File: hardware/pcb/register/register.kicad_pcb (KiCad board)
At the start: 2 copper layers, 62.2 x 21.6 mm, 50 parts, among them J1 Conn_01x08_Male, J2 Conn_01x04_Male, J3 Conn_01x04_Male, J4 Conn_01x04_Male, J5 Conn_01x08_Male, J6 Conn_01x08_Male, U1 74HC245, U2 74HC173, U3 74HC173, U4 74HC173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

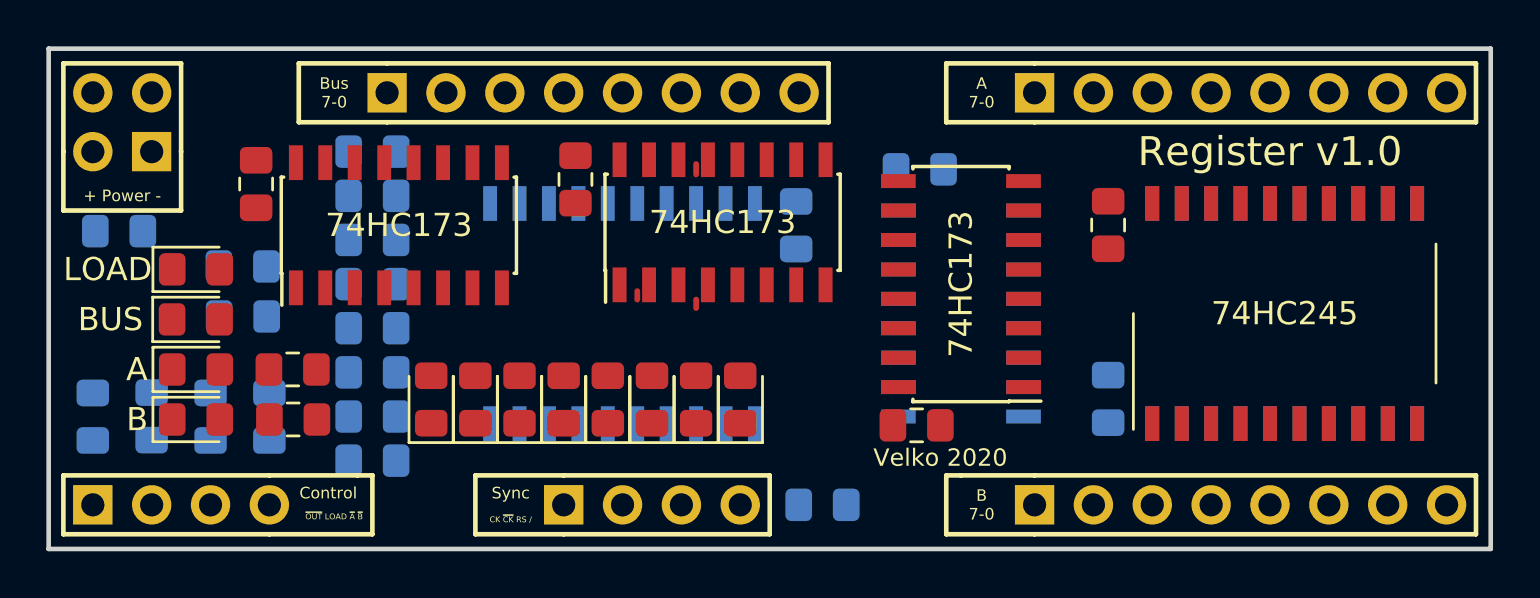
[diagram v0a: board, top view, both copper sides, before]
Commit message: Clean up remaining tracks
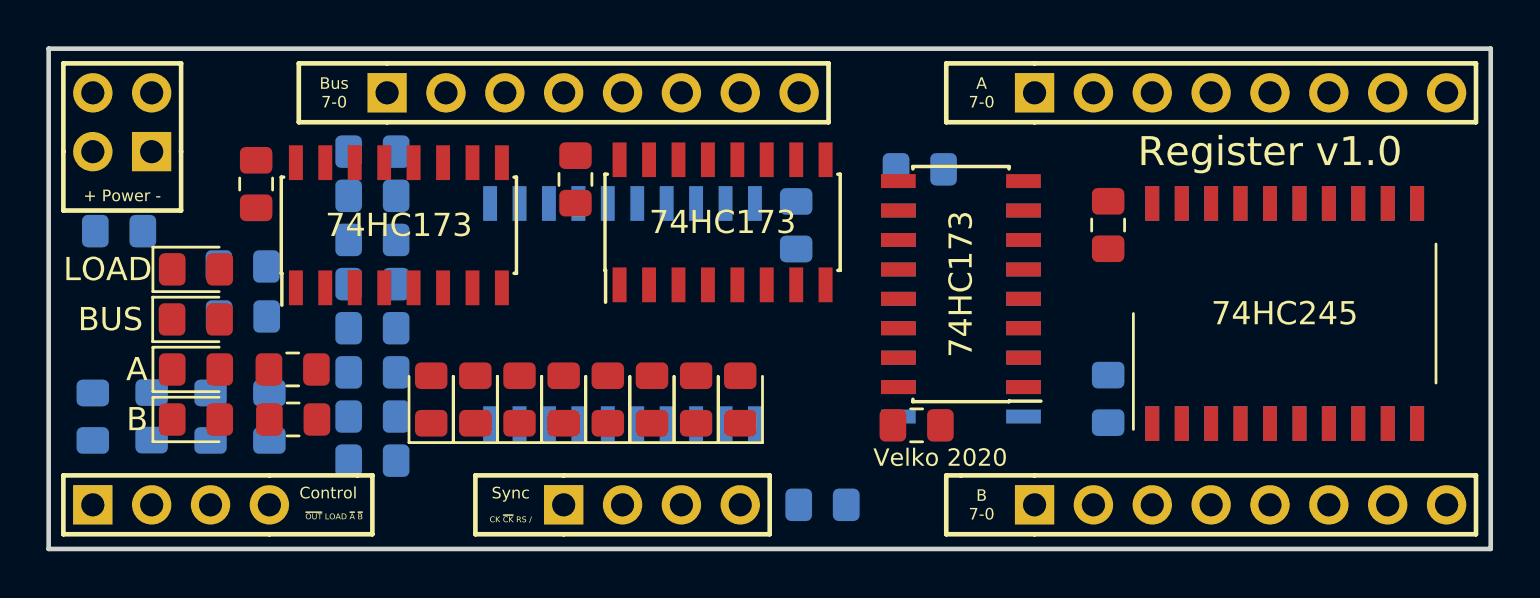
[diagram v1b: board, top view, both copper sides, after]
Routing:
- net A5: track 1.33 -> 0.00 mm
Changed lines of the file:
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@@
     (thickness 1.6)
     (drawings 52)
-    (tracks 11)
+    (tracks 0)
     (zones 0)
     (modules 50)
@@
   (gr_line (start 97.155 36.195) (end 97.155 57.785) (layer Edge.Cuts) (width 0.2))
   (gr_line (start 34.925 36.195) (end 97.155 36.195) (layer Edge.Cuts) (width 0.2))
-  (segment (start 60.325 46.657998) (end 60.325 47.023) (width 0.25) (layer F.Cu) (net 2))
-  (segment (start 53.975 42.875) (end 53.975 42.545) (width 0.25) (layer B.Cu) (net 10))
-  (segment (start 62.865 41.173) (end 62.865 41.623) (width 0.25) (layer F.Cu) (net 15))
-  (segment (start 64.77 38.1) (end 64.75159 38.1) (width 0.25) (layer F.Cu) (net 16))
-  (segment (start 62.865 42.875) (end 62.865 42.545) (width 0.25) (layer B.Cu) (net 17))
-  (segment (start 82.55 38.1) (end 82.55 38.227) (width 0.25) (layer B.Cu) (net 23))
-  (segment (start 83.305 38.1) (end 82.55 38.1) (width 0.25) (layer F.Cu) (net 23))
-  (segment (start 87.63 42.875) (end 87.63 42.425) (width 0.25) (layer F.Cu) (net 23))
-  (segment (start 88.9 52.375) (end 88.9 52.870998) (width 0.25) (layer B.Cu) (net 29))
-  (segment (start 87.665 55.88) (end 87.63 55.88) (width 0.25) (layer B.Cu) (net 30))
-  (segment (start 62.865 47.388002) (end 62.865 47.023) (width 0.25) (layer F.Cu) (net 36))
 )

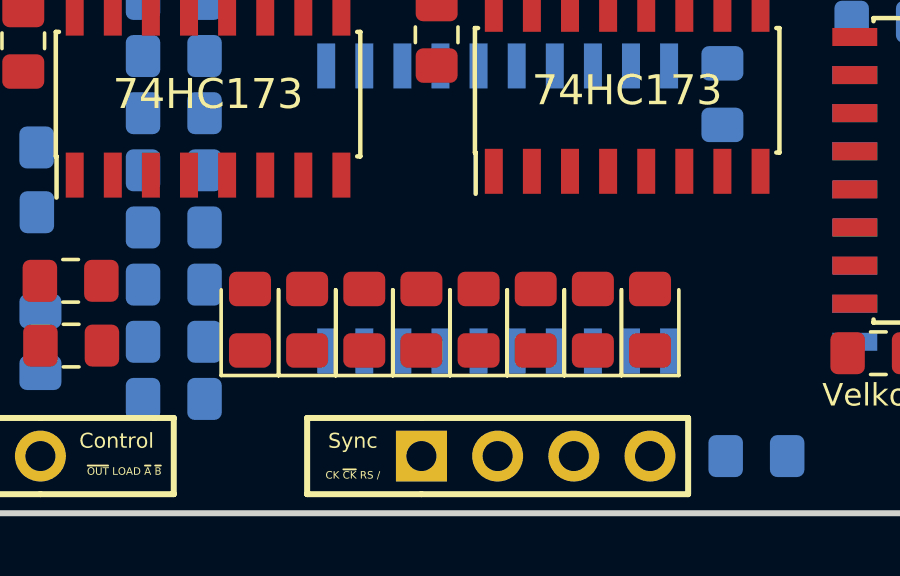
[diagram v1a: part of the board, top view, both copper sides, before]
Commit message: Move LEDs up
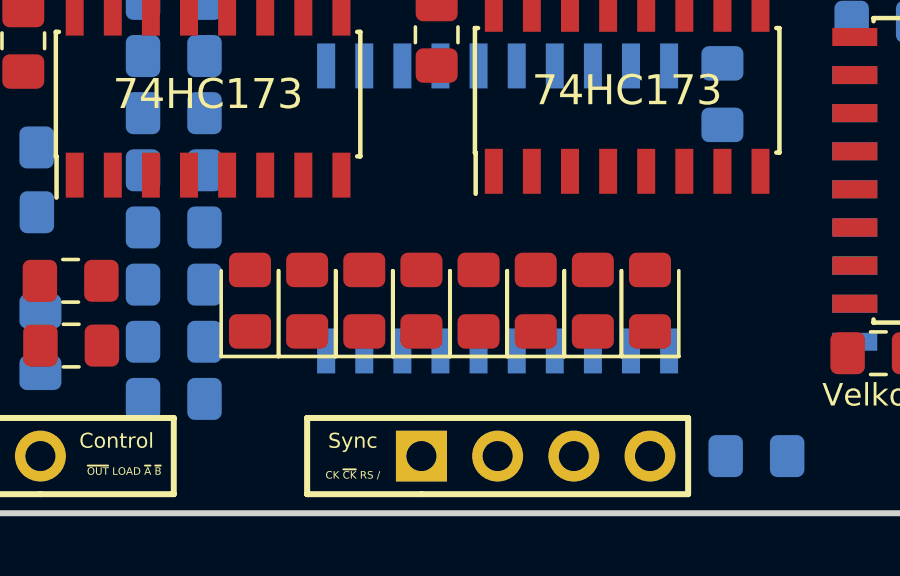
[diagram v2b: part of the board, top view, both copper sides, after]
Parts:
- moved D1 0.63 mm to (64.8, 50.7)
- moved D2 0.63 mm to (62.9, 50.7)
- moved D3 0.63 mm to (61.0, 50.7)
- moved D4 0.63 mm to (59.1, 50.7)
- moved D5 0.63 mm to (57.1, 50.7)
- moved D6 0.63 mm to (55.2, 50.7)
- moved D7 0.63 mm to (53.3, 50.7)
- moved D8 0.63 mm to (51.4, 50.7)
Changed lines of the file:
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@@
   )
   (module LED_SMD:LED_0805_2012Metric_Pad1.15x1.40mm_HandSolder (layer F.Cu)
-    (at 64.77 51.335 90)
+    (at 64.77 50.7 90)
     (descr "LED SMD 0805 (2012 Metric), square (rectangular) end terminal, IPC_7351 nominal, (Body size source: https://docs.google.com/spreadsheets/d/1BsfQQcO9C6DZCsRaXUlFlo91Tg2WpOkGARC1WS5S8t0/edit?usp=sharing), generated with kicad-footprint-generator")
     (tags "LED handsolder")
@@
   )
   (module LED_SMD:LED_0805_2012Metric_Pad1.15x1.40mm_HandSolder (layer F.Cu)
-    (at 62.865 51.335 90)
+    (at 62.865 50.7 90)
     (descr "LED SMD 0805 (2012 Metric), square (rectangular) end terminal, IPC_7351 nominal, (Body size source: https://docs.google.com/spreadsheets/d/1BsfQQcO9C6DZCsRaXUlFlo91Tg2WpOkGARC1WS5S8t0/edit?usp=sharing), generated with kicad-footprint-generator")
     (tags "LED handsolder")
@@
   )
   (module LED_SMD:LED_0805_2012Metric_Pad1.15x1.40mm_HandSolder (layer F.Cu)
-    (at 60.96 51.335 90)
+    (at 60.96 50.7 90)
     (descr "LED SMD 0805 (2012 Metric), square (rectangular) end terminal, IPC_7351 nominal, (Body size source: https://docs.google.com/spreadsheets/d/1BsfQQcO9C6DZCsRaXUlFlo91Tg2WpOkGARC1WS5S8t0/edit?usp=sharing), generated with kicad-footprint-generator")
     (tags "LED handsolder")
@@
   )
   (module LED_SMD:LED_0805_2012Metric_Pad1.15x1.40mm_HandSolder (layer F.Cu)
-    (at 59.055 51.335 90)
+    (at 59.055 50.7 90)
     (descr "LED SMD 0805 (2012 Metric), square (rectangular) end terminal, IPC_7351 nominal, (Body size source: https://docs.google.com/spreadsheets/d/1BsfQQcO9C6DZCsRaXUlFlo91Tg2WpOkGARC1WS5S8t0/edit?usp=sharing), generated with kicad-footprint-generator")
     (tags "LED handsolder")
@@
   )
   (module LED_SMD:LED_0805_2012Metric_Pad1.15x1.40mm_HandSolder (layer F.Cu)
-    (at 57.15 51.335 90)
+    (at 57.15 50.7 90)
     (descr "LED SMD 0805 (2012 Metric), square (rectangular) end terminal, IPC_7351 nominal, (Body size source: https://docs.google.com/spreadsheets/d/1BsfQQcO9C6DZCsRaXUlFlo91Tg2WpOkGARC1WS5S8t0/edit?usp=sharing), generated with kicad-footprint-generator")
     (tags "LED handsolder")
@@
   )
   (module LED_SMD:LED_0805_2012Metric_Pad1.15x1.40mm_HandSolder (layer F.Cu)
-    (at 55.245 51.335 90)
+    (at 55.245 50.7 90)
     (descr "LED SMD 0805 (2012 Metric), square (rectangular) end terminal, IPC_7351 nominal, (Body size source: https://docs.google.com/spreadsheets/d/1BsfQQcO9C6DZCsRaXUlFlo91Tg2WpOkGARC1WS5S8t0/edit?usp=sharing), generated with kicad-footprint-generator")
     (tags "LED handsolder")
@@
   )
   (module LED_SMD:LED_0805_2012Metric_Pad1.15x1.40mm_HandSolder (layer F.Cu)
-    (at 53.34 51.335 90)
+    (at 53.34 50.7 90)
     (descr "LED SMD 0805 (2012 Metric), square (rectangular) end terminal, IPC_7351 nominal, (Body size source: https://docs.google.com/spreadsheets/d/1BsfQQcO9C6DZCsRaXUlFlo91Tg2WpOkGARC1WS5S8t0/edit?usp=sharing), generated with kicad-footprint-generator")
     (tags "LED handsolder")
@@
   )
   (module LED_SMD:LED_0805_2012Metric_Pad1.15x1.40mm_HandSolder (layer F.Cu)
-    (at 51.435 51.335 90)
-    (descr "LED SMD 0805 (2012 Metric), square (rectangular) end terminal, IPC_7351 nominal, (Body size source: https://docs.google.com/spreadsheets/d/1BsfQQcO9C6DZCsRaXUlFlo91Tg2WpOkGARC1WS5S8t0/edit?usp=sharing), generated with kicad-footprint-generator")
-    (tags "LED handsolder")
+    (at 51.435 50.7 90)
+    (descr "LED SMD 0805 (2012 Metric), square (rectangular) end terminal, IPC_7351 nominal, (Body size source: https://docs.google.com/spreadsheets/d/1BsfQQcO9C6DZCsRaXUlFlo91Tg2WpOkGARC1WS5S8t0/edit?usp=sharing), generated with kicad-footprint-generator")
+    (tags "LED handsolder")

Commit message: Switch bus output chip to M taps
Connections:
- U1 pad 2: TAP0 -> M0
- U1 pad 3: TAP1 -> M1
- U1 pad 4: TAP2 -> M2
- U1 pad 5: TAP3 -> M3
- U1 pad 6: TAP4 -> M4
- U1 pad 7: TAP5 -> M5
- U1 pad 8: TAP6 -> M6
- U1 pad 9: TAP7 -> M7
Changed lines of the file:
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@@
     )
     (pad 6 smd rect (at -4.75 -0.635 90) (size 1.5 0.6) (layers B.Cu B.Paste B.Mask)
-      (net 56 TAP4))
+      (net 38 M4))
     (pad 5 smd rect (at -4.75 0.635 90) (size 1.5 0.6) (layers B.Cu B.Paste B.Mask)
-      (net 55 TAP3))
+      (net 37 M3))
     (pad 4 smd rect (at -4.75 1.905 90) (size 1.5 0.6) (layers B.Cu B.Paste B.Mask)
-      (net 60 TAP2))
+      (net 36 M2))
     (pad 3 smd rect (at -4.75 3.175 90) (size 1.5 0.6) (layers B.Cu B.Paste B.Mask)
-      (net 61 TAP1))
+      (net 35 M1))
     (pad 2 smd rect (at -4.75 4.445 90) (size 1.5 0.6) (layers B.Cu B.Paste B.Mask)
-      (net 62 TAP0))
+      (net 34 M0))
     (pad 1 smd rect (at -4.75 5.715 90) (size 1.5 0.6) (layers B.Cu B.Paste B.Mask)
       (net 1 VCC))
     (pad 7 smd rect (at -4.75 -1.905 90) (size 1.5 0.6) (layers B.Cu B.Paste B.Mask)
-      (net 57 TAP5))
+      (net 39 M5))
     (pad 8 smd rect (at -4.75 -3.175 90) (size 1.5 0.6) (layers B.Cu B.Paste B.Mask)
-      (net 58 TAP6))
+      (net 40 M6))
     (pad 9 smd rect (at -4.75 -4.445 90) (size 1.5 0.6) (layers B.Cu B.Paste B.Mask)
-      (net 59 TAP7))
+      (net 41 M7))
     (pad 10 smd rect (at -4.75 -5.715 90) (size 1.5 0.6) (layers B.Cu B.Paste B.Mask)
       (net 2 GND))

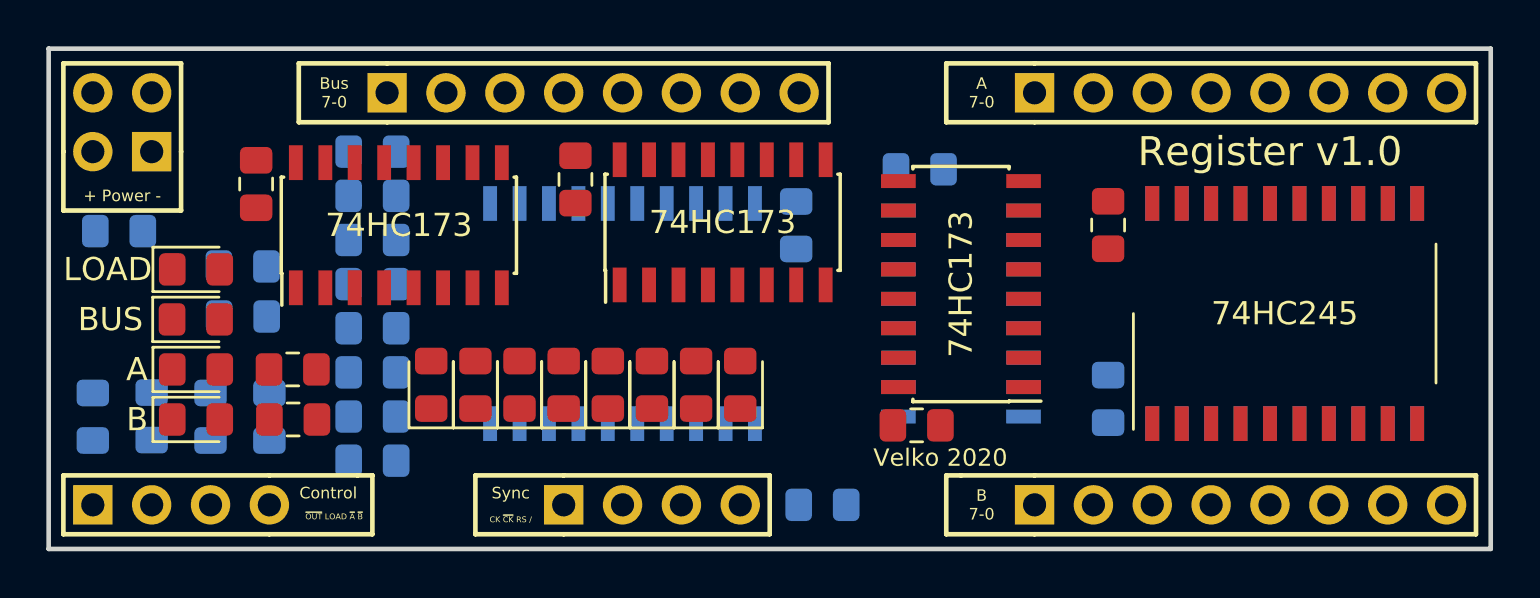
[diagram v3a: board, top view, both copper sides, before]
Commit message: Import autorouted
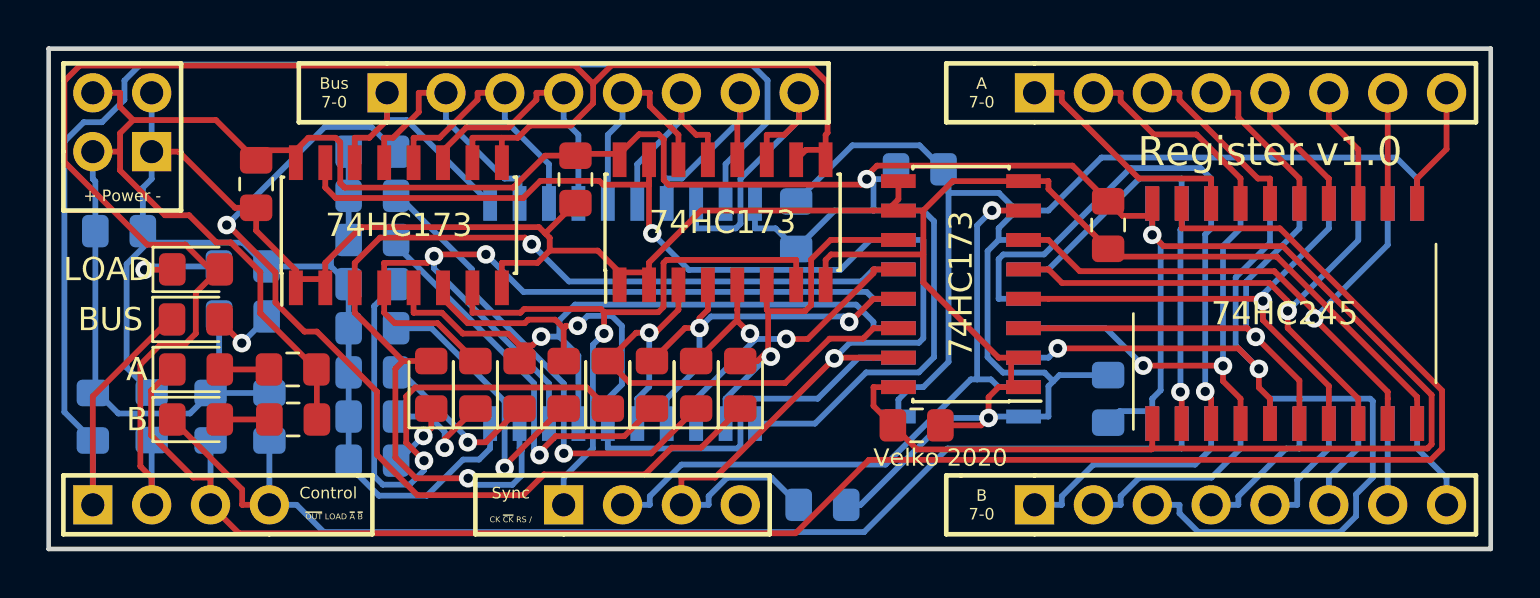
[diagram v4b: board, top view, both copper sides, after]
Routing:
- net GND: track 0.00 -> 210.1 mm, vias 0 -> 1
- net VCC: track 0.00 -> 181.4 mm, vias 0 -> 2
- net ~A_OUT~: track 0.00 -> 83.4 mm
- net LOAD: track 0.00 -> 75.0 mm
- net ~BUS_OUT~: track 0.00 -> 64.2 mm
- net RESET: track 0.00 -> 59.1 mm, vias 0 -> 2
- net ~B_OUT~: track 0.00 -> 51.3 mm
- net M7: track 0.00 -> 43.9 mm, vias 0 -> 2
- net Net-(D1-Pad1): track 0.00 -> 40.4 mm, vias 0 -> 1
- net M6: track 0.00 -> 39.4 mm, vias 0 -> 2
- net M4: track 0.00 -> 31.5 mm, vias 0 -> 1
- net M5: track 0.00 -> 29.1 mm, vias 0 -> 1
- net ~CLK~: track 0.00 -> 28.8 mm, vias 0 -> 1
- net CLK: track 0.00 -> 27.3 mm, vias 0 -> 1
- net TAP0: track 0.00 -> 26.3 mm, vias 0 -> 1
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
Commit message: Manual touch-up
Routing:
- net RESET: track 59.1 -> 58.2 mm
- net A7: track 10.4 -> 11.2 mm
- net B3: track 5.25 -> 4.62 mm
- net A4: track 7.04 -> 6.42 mm
